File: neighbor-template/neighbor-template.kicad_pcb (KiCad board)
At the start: 4 copper layers, 70.7 x 53.3 mm, 7 parts, among them J1 NEIGHBOR1, J2 NEIGHBOR2, J7 BONUS_ROW

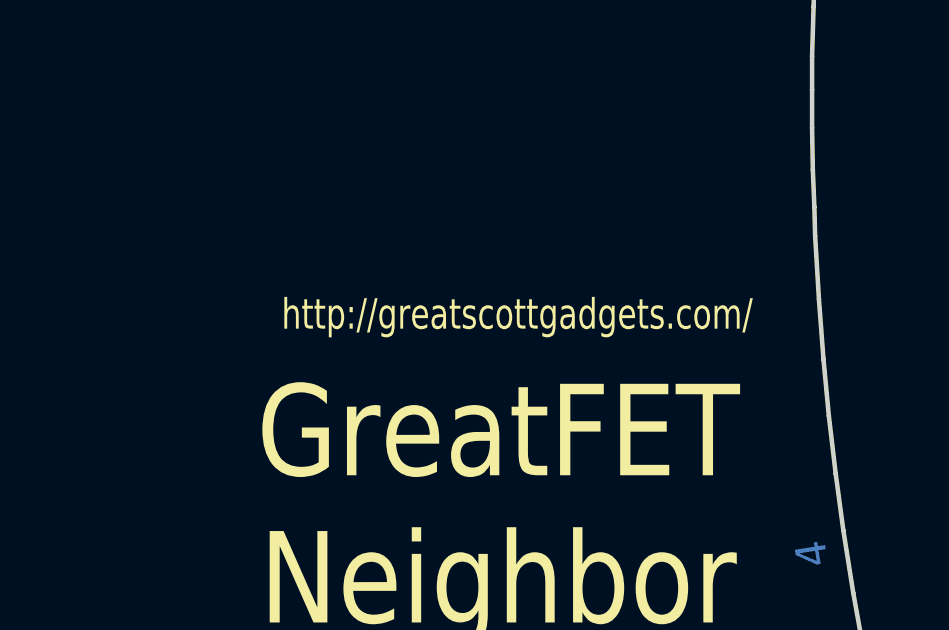
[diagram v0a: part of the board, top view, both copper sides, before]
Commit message: minor updates to neighbor template
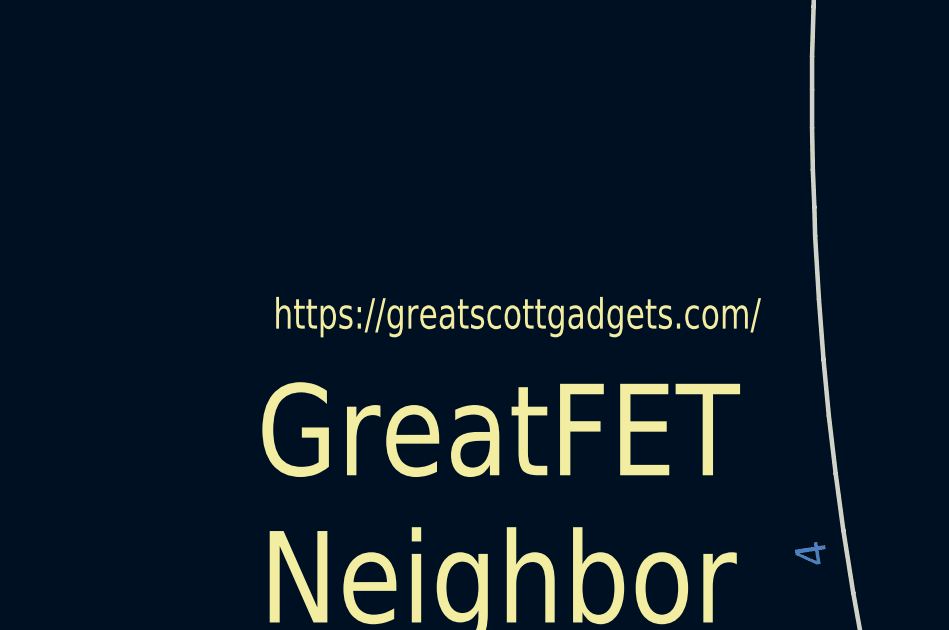
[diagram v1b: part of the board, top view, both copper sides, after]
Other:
- board text added: "https://greatscottgadgets.com/"
- board text removed: "http://greatscottgadgets.com/"
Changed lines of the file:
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@@
     (effects (font (size 1.016 1.016) (thickness 0.1778)))
   )
-  (gr_text http://greatscottgadgets.com/ (at 168.021 102.616) (layer F.SilkS)
+  (gr_text https://greatscottgadgets.com/ (at 168.021 102.616) (layer F.SilkS)
     (effects (font (size 1.016 0.762) (thickness 0.1524)))
   )
